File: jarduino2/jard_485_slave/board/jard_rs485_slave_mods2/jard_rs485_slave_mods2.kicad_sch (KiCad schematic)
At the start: 0 parts

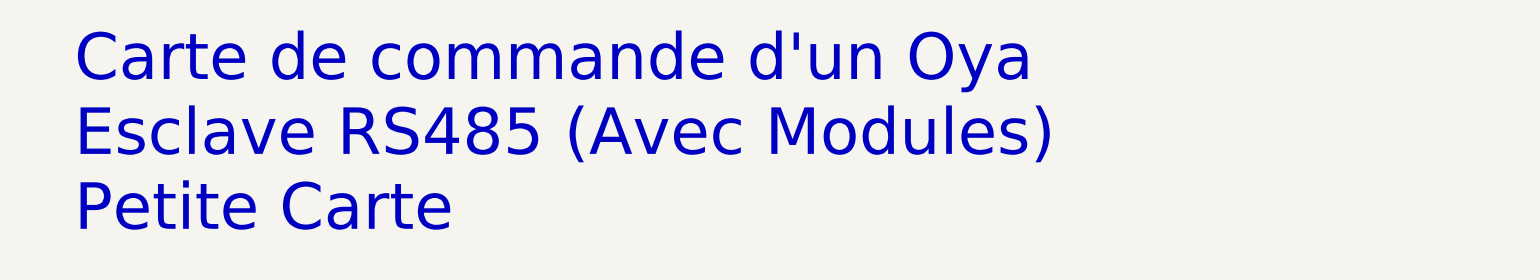
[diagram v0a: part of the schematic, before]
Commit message: Suppression du module RS485 et remplacement par le CI MAX485E lui-même. Preparation version G...
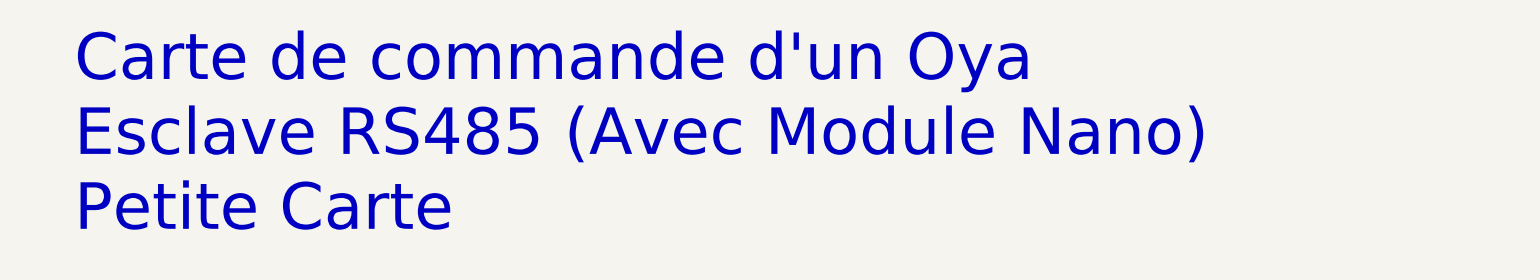
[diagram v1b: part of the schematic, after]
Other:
- note added: "Carte de commande d'un Oya Esclave RS485 (Avec Module Nano) Petite Carte"
- note removed: "Carte de commande d'un Oya Esclave RS485 (Avec Modules) Petite Carte"
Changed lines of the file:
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@@
   (title_block
     (title "Carte de commande d'un OYA - Esclave RS485")
-    (date "2024-05-04")
-    (rev "F0")
+    (date "2024-05-05")
+    (rev "G0")
     (company "BPC")
-    (comment 1 "Technologie avec modules Arduino / Petite carte")
+    (comment 1 "Technologie avec modules Arduino Nano / Petite carte")
     (comment 2 "Monitoring de tension d'alimentation")
     (comment 3 "1 sortie 12V/5A - 2 entrées TOR - 1 débimètre - 1 LED - Temp - RS485")
@@
     (effects (font (size 1.27 1.27)) (justify left top))
   )
-  (text "Carte de commande d'un Oya\nEsclave RS485 (Avec Modules)\nPetite Carte"
+  (text "Carte de commande d'un Oya\nEsclave RS485 (Avec Module Nano)\nPetite Carte"
     (at 46.99 71.12 0)
     (effects (font (face "Arial") (size 10 10)) (justify left bottom))
